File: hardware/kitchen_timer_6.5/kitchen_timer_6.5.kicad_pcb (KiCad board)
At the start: 2 copper layers, 79.5 x 66 mm, 57 parts, among them J1 JST PH 2.0, J2 USB_C, J3 BREAKOUT, Q1 MMBT2222A, Q2 MMBT2222A, Q3 MMBT2222A, Q4 MMBT2222A, Q5 MMBT2222A, SW1 ON/OFF, SW2 SECONDS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

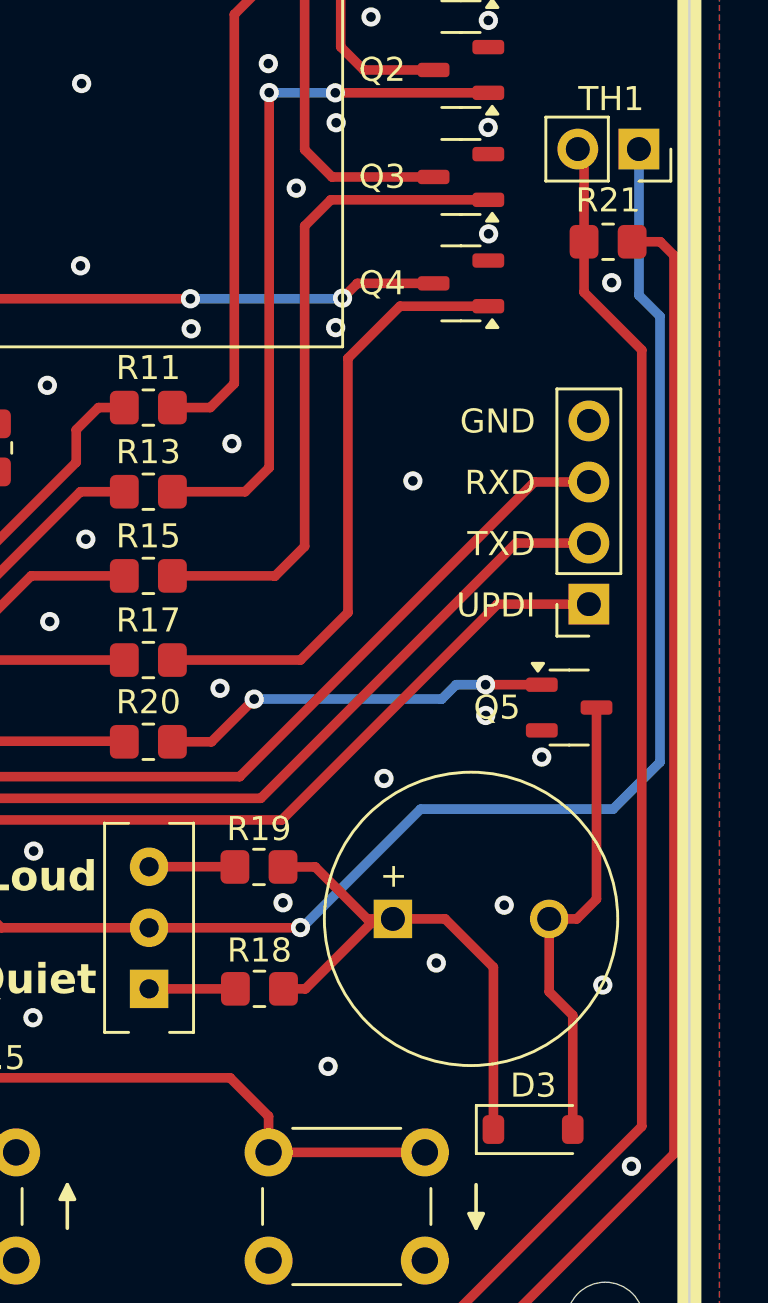
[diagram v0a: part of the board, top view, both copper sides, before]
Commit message: converted temp_gnd to temp_vcc and change temperature reading logic
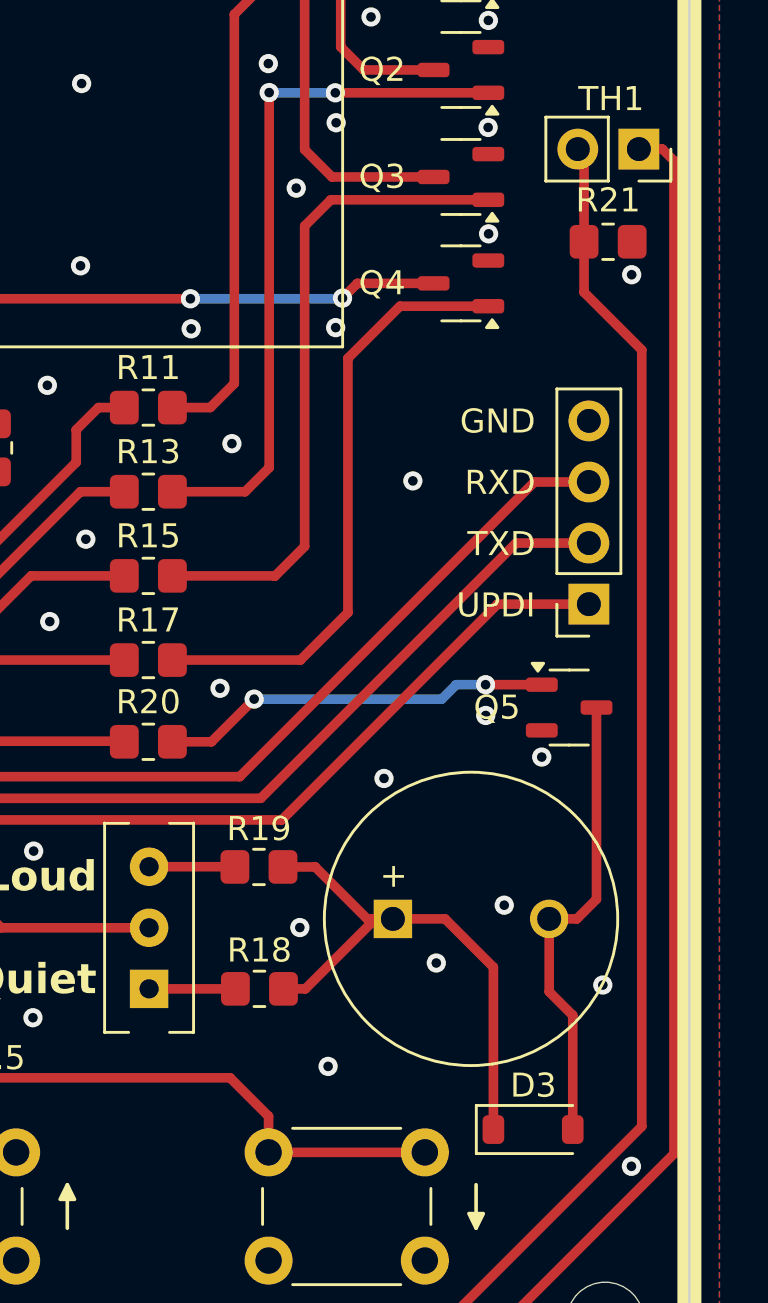
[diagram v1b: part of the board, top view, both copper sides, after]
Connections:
- R21 pad 1: /TEMP_GND -> GND
- TH1 pad 1: +5V -> /TEMP_VCC
- U2 pad 23: /TEMP_GND -> /TEMP_VCC
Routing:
- net /TEMP_VCC: track 0.00 -> 133.1 mm, vias 0 -> 2
- net /TEMP_GND: track 129.5 -> 0.00 mm, vias 2 -> 0
- net +5V: track 146.3 -> 96.3 mm, vias 6 -> 5
